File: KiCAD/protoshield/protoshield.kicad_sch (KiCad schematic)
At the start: 35 parts, among them J1 Screw_Terminal_01x03, J2 Screw_Terminal_01x02, J3 Screw_Terminal_01x02, J4 Screw_Terminal_01x02, J5 Screw_Terminal_01x02, J6 Screw_Terminal_01x03, J7 Screw_Terminal_01x04, J8 Screw_Terminal_01x04, U2 Metro_ESP32S3

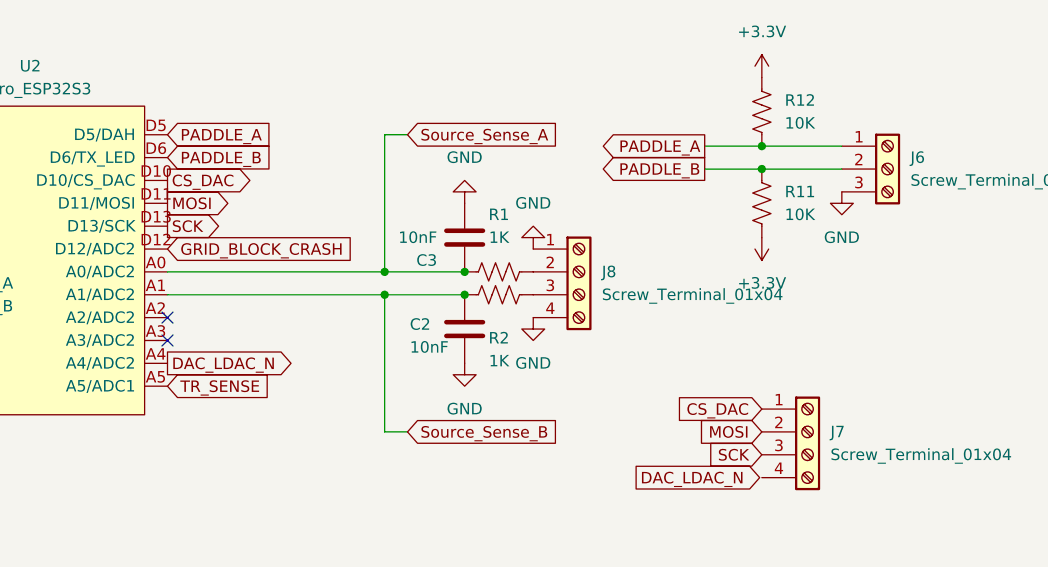
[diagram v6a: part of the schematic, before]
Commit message: KiCad revC: protoshield minor wiring edits
Small adjustments to protoshield schematic — added a couple of
wires, removed a no_connect that's no longer needed. Updated
used_designators tracking to J8 and #PWR23.

Co-Authored-By: Claude Opus 4.7 <noreply@anthropic.com>
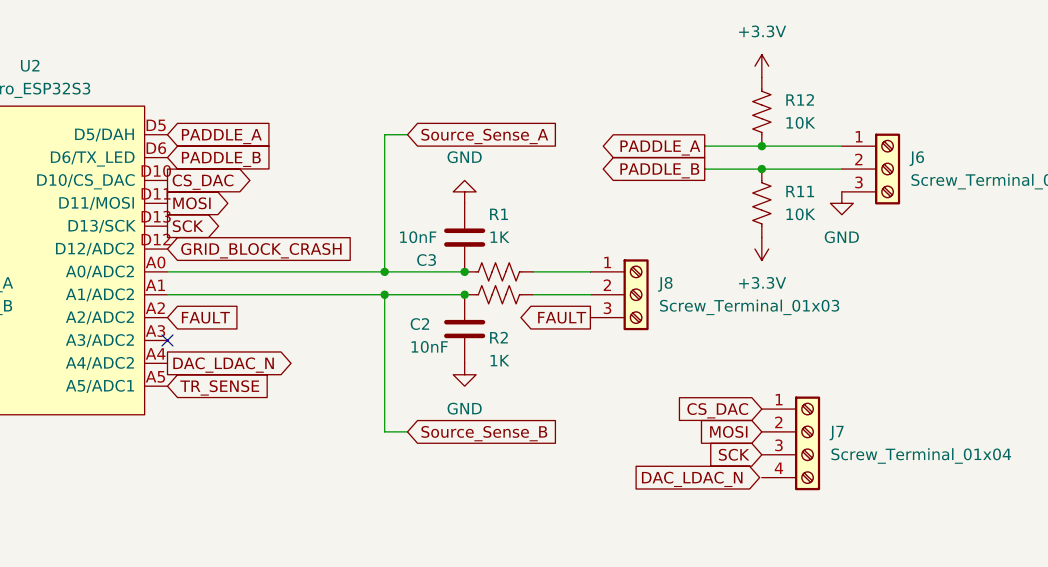
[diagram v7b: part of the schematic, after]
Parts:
- removed J8: Screw_Terminal_01x04, symbol Connector:Screw_Terminal_01x04
- added J8: Screw_Terminal_01x03, symbol Connector:Screw_Terminal_01x03
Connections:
- net at R2.2: now also J8.2 (Pin_2)
- net at R1.2: now also J8.1 (Pin_1)
- net FAULT: now reaches U2.A2 (A2/ADC2)
- net FAULT: now also J8.3 (Pin_3)
- no-connect marks 6 -> 5
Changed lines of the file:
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@@
 	)
 	(no_connect
-		(at 161.29 91.44)
-	)
-	(no_connect
 		(at 161.29 93.98)
 	)
@@
 	(wire
 		(pts
+			(xy 208.28 86.36) (xy 201.93 86.36)
+		)
+		(stroke
+			(width 0)
+			(type default)
+		)
+	)
+	(wire
+		(pts
 			(xy 185.42 88.9) (xy 194.31 88.9)
 		)
@@
 	(wire
 		(pts
+			(xy 208.28 88.9) (xy 201.93 88.9)
+		)
+		(stroke
+			(width 0)
+			(type default)
+		)
+	)
+	(wire
+		(pts
 			(xy 55.88 161.29) (xy 57.15 161.29)
 		)
@@
 		)
 	)
+	(global_label "FAULT"
+		(shape input)
+		(at 161.29 91.44 0)
+		(fields_autoplaced yes)
+		(effects
+			(font
+				(size 1.27 1.27)
+			)
+			(justify left)
+		)
+		(property "Intersheetrefs" "${INTERSHEET_REFS}"
+			(at 169.7786 91.44 0)
+			(hide yes)
+			(show_name no)
+			(do_not_autoplace no)
+			(effects
+				(font
+					(size 1.27 1.27)
+				)
+				(justify left)
+			)
+		)
+	)
 	(global_label "Source_Sense_A"
 		(shape input)
@@
 		)
 	)
+	(global_label "FAULT"
+		(shape output)
+		(at 208.28 91.44 180)
+		(fields_autoplaced yes)
+		(effects
+			(font
+				(size 1.27 1.27)
+			)
+			(justify right)
+		)
+		(property "Intersheetrefs" "${INTERSHEET_REFS}"
+			(at 199.7914 91.44 0)
+			(hide yes)
+			(show_name no)
+			(do_not_autoplace no)
+			(effects
+				(font
+					(size 1.27 1.27)
+				)
+				(justify right)
+			)
+		)
+	)
 	(global_label "MOSI"
 		(shape output)
@@
 	)
 	(symbol
-		(lib_id "power:GND")
-		(at 201.93 83.82 180)
-		(unit 1)
-		(body_style 1)
-		(exclude_from_sim no)
-		(in_bom yes)
-		(on_board yes)
-		(in_pos_files yes)
-		(dnp no)
-		(fields_autoplaced yes)
-		(property "Reference" "#PWR024"
-			(at 201.93 77.47 0)
-			(hide yes)
-			(show_name no)
-			(do_not_autoplace no)
-			(effects
-				(font
-					(size 1.27 1.27)
-				)
-			)
-		)
-		(property "Value" "GND"
-			(at 201.93 78.74 0)
-			(show_name no)
-			(do_not_autoplace no)
-			(effects
-				(font
-					(size 1.27 1.27)
-				)
-			)
-		)
-		(property "Footprint" ""
-			(at 201.93 83.82 0)
-			(hide yes)
-			(show_name no)
-			(do_not_autoplace no)
-			(effects
-				(font
-					(size 1.27 1.27)
-				)
-			)
-		)
-		(property "Datasheet" ""
-			(at 201.93 83.82 0)
-			(hide yes)
-			(show_name no)
-			(do_not_autoplace no)
-			(effects
-				(font
-					(size 1.27 1.27)
-				)
-			)
-		)
-		(property "Description" "Power symbol creates a global label with name \"GND\" , ground"
-			(at 201.93 83.82 0)
-			(hide yes)
-			(show_name no)
-			(do_not_autoplace no)
-			(effects
-				(font
-					(size 1.27 1.27)
-				)
-			)
-		)
-		(pin "1"
-		)
-		(instances
-			(project "protoshield"
-				(path "/90f14230-179e-419d-8d57-3db6b8a7c39f"
-					(reference "#PWR024")
-					(unit 1)
-				)
-			)
-		)
-	)
-	(symbol
 		(lib_id "Connector:Screw_Terminal_01x02")
 		(at 27.94 125.73 180)
@@
 	)
 	(symbol
-		(lib_id "power:GND")
-		(at 201.93 91.44 0)
-		(unit 1)
-		(body_style 1)
-		(exclude_from_sim no)
-		(in_bom yes)
-		(on_board yes)
-		(in_pos_files yes)
-		(dnp no)
-		(fields_autoplaced yes)
-		(property "Reference" "#PWR023"
-			(at 201.93 97.79 0)
-			(hide yes)
-			(show_name no)
-			(do_not_autoplace no)
-			(effects
-				(font
-					(size 1.27 1.27)
-				)
-			)
-		)
-		(property "Value" "GND"
-			(at 201.93 96.52 0)
-			(show_name no)
-			(do_not_autoplace no)
-			(effects
-				(font
-					(size 1.27 1.27)
-				)
-			)
-		)
-		(property "Footprint" ""
-			(at 201.93 91.44 0)
-			(hide yes)
-			(show_name no)
-			(do_not_autoplace no)
-			(effects
-				(font
-					(size 1.27 1.27)
-				)
-			)
-		)
-		(property "Datasheet" ""
-			(at 201.93 91.44 0)
-			(hide yes)
-			(show_name no)
-			(do_not_autoplace no)
-			(effects
-				(font
-					(size 1.27 1.27)
-				)
-			)
-		)
-		(property "Description" "Power symbol creates a global label with name \"GND\" , ground"
-			(at 201.93 91.44 0)
-			(hide yes)
-			(show_name no)
-			(do_not_autoplace no)
-			(effects
-				(font
-					(size 1.27 1.27)
-				)
-			)
-		)
-		(pin "1"
-		)
-		(instances
-			(project "protoshield"
-				(path "/90f14230-179e-419d-8d57-3db6b8a7c39f"
-					(reference "#PWR023")
-					(unit 1)
-				)
-			)
-		)
-	)
-	(symbol
 		(lib_id "Device:R_US")
 		(at 38.1 53.34 90)
@@
 	)
 	(symbol
-		(lib_id "Connector:Screw_Terminal_01x04")
-		(at 207.01 86.36 0)
-		(unit 1)
-		(body_style 1)
-		(exclude_from_sim no)
-		(in_bom yes)
-		(on_board yes)
-		(in_pos_files yes)
-		(dnp no)
-		(fields_autoplaced yes)
-		(property "Reference" "J8"
-			(at 209.55 86.3599 0)
-			(show_name no)
-			(do_not_autoplace no)
-			(effects
-				(font
-					(size 1.27 1.27)
-				)
-				(justify left)
-			)
-		)
-		(property "Value" "Screw_Terminal_01x04"
-			(at 209.55 88.8999 0)
-			(show_name no)
-			(do_not_autoplace no)
-			(effects
-				(font
-					(size 1.27 1.27)
-				)
-				(justify left)
-			)
-		)
-		(property "Footprint" ""
-			(at 207.01 86.36 0)
-			(hide yes)
-			(show_name no)
-			(do_not_autoplace no)
-			(effects
-				(font
-					(size 1.27 1.27)
-				)
-			)
-		)
-		(property "Datasheet" ""
-			(at 207.01 86.36 0)
-			(hide yes)
-			(show_name no)
-			(do_not_autoplace no)
-			(effects
-				(font
-					(size 1.27 1.27)
-				)
-			)
-		)
-		(property "Description" "Generic screw terminal, single row, 01x04, script generated (kicad-library-utils/schlib/autogen/connector/)"
-			(at 207.01 86.36 0)
-			(hide yes)
-			(show_name no)
-			(do_not_autoplace no)
-			(effects
-				(font
-					(size 1.27 1.27)
-				)
-			)
-		)
-		(pin "1"
-		)
-		(pin "3"
-		)
-		(pin "4"
-		)
-		(pin "2"
-		)
-		(instances
-			(project "protoshield"
-				(path "/90f14230-179e-419d-8d57-3db6b8a7c39f"
-					(reference "J8")
-					(unit 1)
-				)
-			)
-		)
-	)
-	(symbol
 		(lib_id "power:GND")
 		(at 44.45 63.5 0)
@@
 					(unit 1)
 				)
+			)
+		)
+	)
+	(symbol
+		(lib_id "Connector:Screw_Terminal_01x03")
+		(at 213.36 88.9 0)
+		(unit 1)
+		(body_style 1)
+		(exclude_from_sim no)
+		(in_bom yes)
+		(on_board yes)
+		(in_pos_files yes)
+		(dnp no)
+		(fields_autoplaced yes)
+		(property "Reference" "J8"
+			(at 215.9 87.6299 0)
+			(show_name no)
+			(do_not_autoplace no)
+			(effects
+				(font
+					(size 1.27 1.27)
+				)
+				(justify left)
+			)
+		)
+		(property "Value" "Screw_Terminal_01x03"
+			(at 215.9 90.1699 0)
+			(show_name no)
+			(do_not_autoplace no)
+			(effects
+				(font
+					(size 1.27 1.27)
+				)
+				(justify left)
+			)
+		)
+		(property "Footprint" ""
+			(at 213.36 88.9 0)
+			(hide yes)
+			(show_name no)
+			(do_not_autoplace no)
+			(effects
+				(font
+					(size 1.27 1.27)
+				)
+			)
+		)
+		(property "Datasheet" ""
+			(at 213.36 88.9 0)
+			(hide yes)
+			(show_name no)
+			(do_not_autoplace no)
+			(effects
+				(font
+					(size 1.27 1.27)
+				)
+			)
+		)
+		(property "Description" "Generic screw terminal, single row, 01x03, script generated (kicad-library-utils/schlib/autogen/connector/)"
+			(at 213.36 88.9 0)
+			(hide yes)
+			(show_name no)
+			(do_not_autoplace no)
+			(effects
+				(font
+					(size 1.27 1.27)
+				)
+			)
+		)
+		(pin "3"
+		)
+		(pin "1"
+		)
+		(pin "2"
+		)
+		(instances
+			(project "protoshield"
+				(path "/90f14230-179e-419d-8d57-3db6b8a7c39f"
+					(reference "J8")
+					(unit 1)
+				)

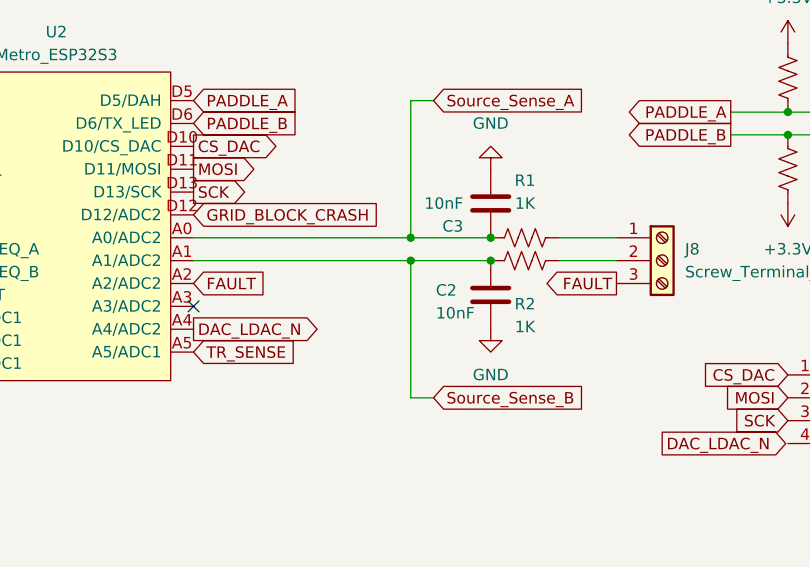
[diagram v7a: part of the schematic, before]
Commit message: KiCad revC: resolve project-audit findings on analog + protoshield
Fixes the four items from Documentation/2026-10-11-project-audit.md
plus the follow-up Q11 series-R finding:

- Rename FAULT -> FAULT_N on analog arduino and protoshield to match
  ss_pa (active-low per the latest design spec in ss_pa.md)
- Delete the stale PA_OUTPUT_LEVEL global label on dac sheet
  (tube-era signal, no consumer; MCP4922 VoutA now unused and output
  connector marked DNP)
- Fix ENC_INT_CLEAN -> R6 -> ENC_INT signal path on analog arduino
  so the encoder interrupt actually reaches the Metro via protoshield
- Re-export analog.net so it reflects the current schematic (J31
  RJ45 to ss_pa, bias/sense/fault signals, R6 wiring, etc.)

Co-Authored-By: Claude Opus 4.7 <noreply@anthropic.com>
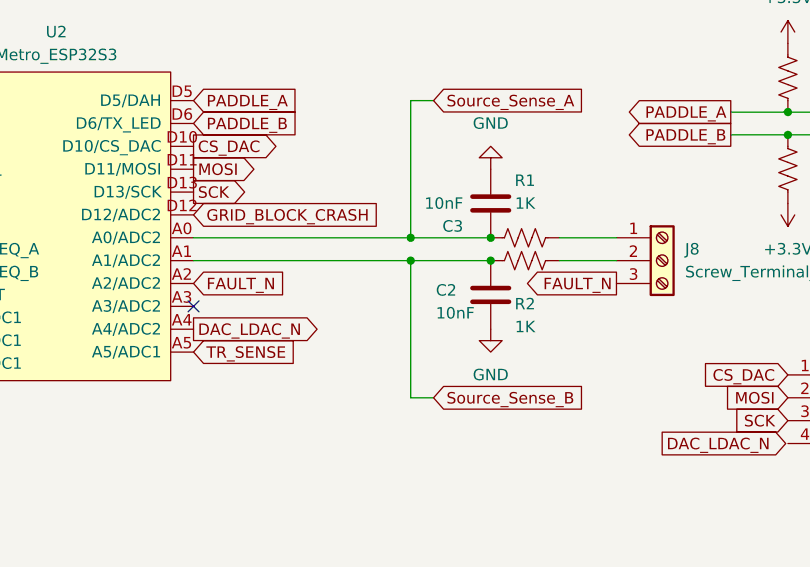
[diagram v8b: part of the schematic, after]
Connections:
- net FAULT renamed FAULT_N
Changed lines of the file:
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@@
 		)
 	)
-	(global_label "FAULT"
+	(global_label "FAULT_N"
 		(shape input)
 		(at 161.29 91.44 0)
@@
 		)
 		(property "Intersheetrefs" "${INTERSHEET_REFS}"
-			(at 169.7786 91.44 0)
+			(at 172.0767 91.44 0)
 			(hide yes)
 			(show_name no)
@@
 		)
 	)
-	(global_label "FAULT"
+	(global_label "FAULT_N"
 		(shape output)
 		(at 208.28 91.44 180)
@@
 		)
 		(property "Intersheetrefs" "${INTERSHEET_REFS}"
-			(at 199.7914 91.44 0)
-			(hide yes)
-			(show_name no)
+			(at 197.4933 91.44 0)
+			(hide yes)
+			(show_name no)
